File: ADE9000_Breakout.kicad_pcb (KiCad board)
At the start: 2 copper layers, 38.1 x 38 mm, 61 parts, among them J1 SPI JST-SH, J2 Current In, J3 Voltage In, U1 ADE9000, Y1 24.576MHz

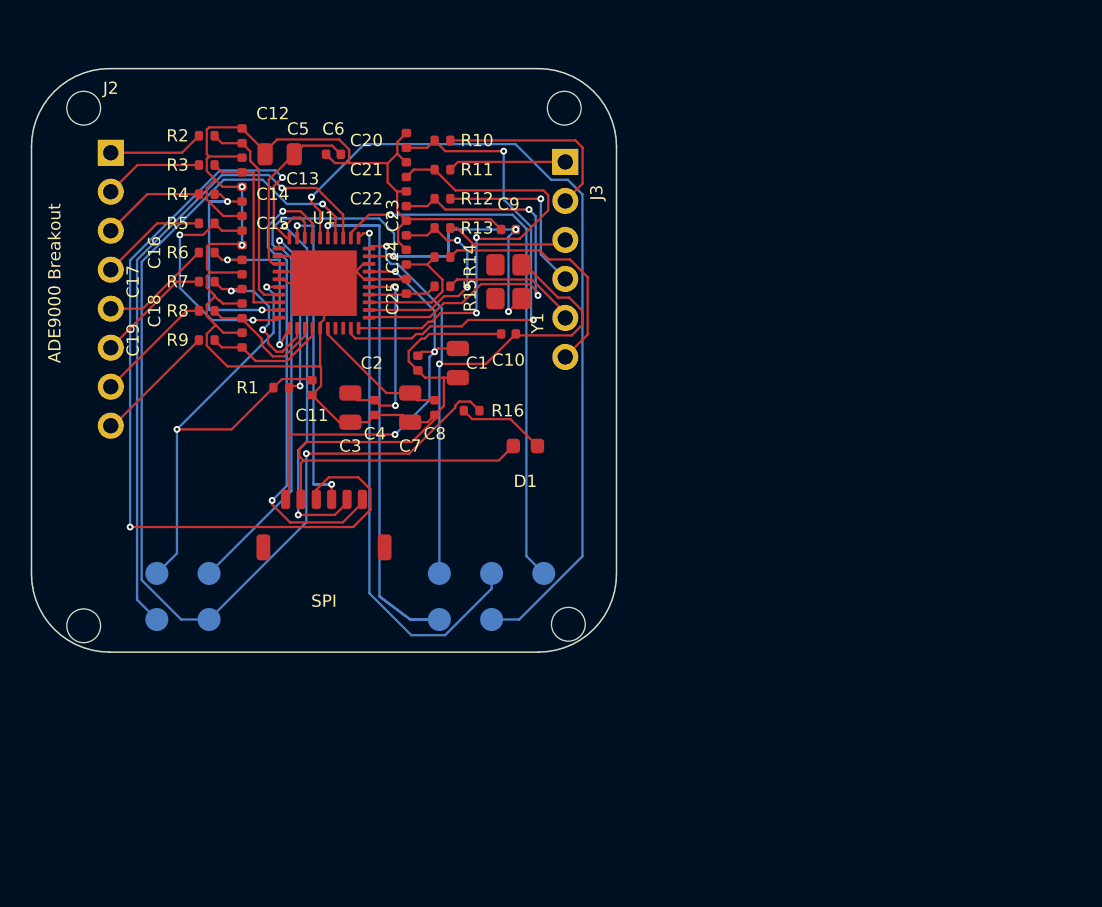
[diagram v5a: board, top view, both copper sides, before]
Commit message: Relayout using connectors for analog inputs
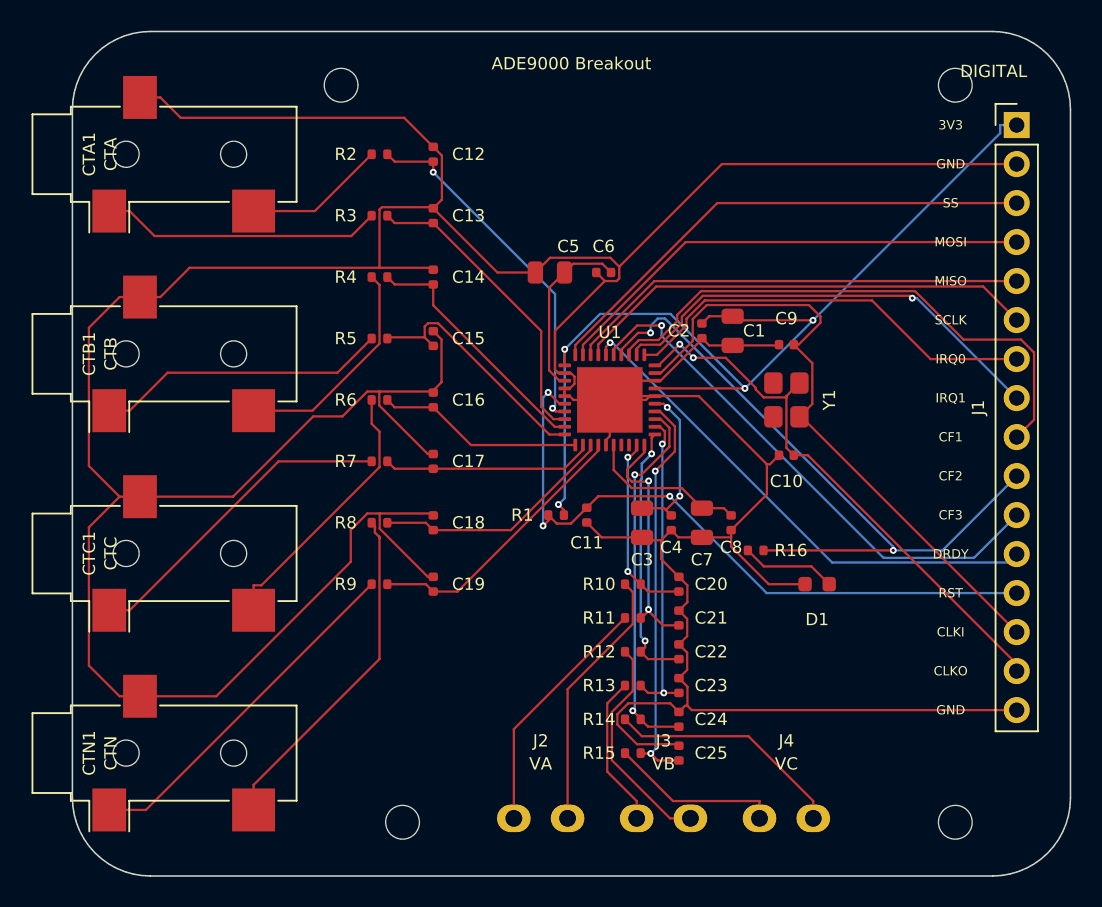
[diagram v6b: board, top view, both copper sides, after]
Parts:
- removed TP10: CF4_DREADY, TestPoint:TestPoint_Pad_D1.5mm
- removed TP11: RESET, TestPoint:TestPoint_Pad_D1.5mm
- removed TP12: CLKIN, TestPoint:TestPoint_Pad_D1.5mm
- removed TP13: CLKOUT, TestPoint:TestPoint_Pad_D1.5mm
- removed TP5: IRQ0, TestPoint:TestPoint_Pad_D1.5mm
- removed TP6: IRQ1, TestPoint:TestPoint_Pad_D1.5mm
- removed TP7: CF1, TestPoint:TestPoint_Pad_D1.5mm
- removed TP8: CF2, TestPoint:TestPoint_Pad_D1.5mm
- removed TP9: CF3_ZX, TestPoint:TestPoint_Pad_D1.5mm
- added CTA1: CT stereo, Jack_3.5mm_CUI_SJ-3523-SMT_Horizontal, F.Cu at (129.5, 88.0)
- added CTB1: CT stereo, Jack_3.5mm_CUI_SJ-3523-SMT_Horizontal, F.Cu at (129.5, 101.0)
- added CTC1: CT stereo, Jack_3.5mm_CUI_SJ-3523-SMT_Horizontal, F.Cu at (129.5, 114.0)
- added CTN1: CT stereo, Jack_3.5mm_CUI_SJ-3523-SMT_Horizontal, F.Cu at (129.5, 127.0)
- added J4: Voltage, TerminalBlock_4Ucon:TerminalBlock_4Ucon_1x02_P3.50mm_Horizontal, F.Cu at (170.0, 131.2)
- J1: value SPI JST-SH -> DIGITAL; footprint JST_SHL_SM06B-SHLS-TF_1x06-1MP_P1.00mm_Horizontal -> PinHeader_1x16_P2.54mm_Vertical
- J2: value Current In -> Voltage; footprint Connector_PinHeader_2.54mm:PinHeader_1x08_P2.54mm_Vertical -> TerminalBlock_4Ucon:TerminalBlock_4Ucon_1x02_P3.50mm_Horizontal
- J3: value Voltage In -> Voltage; footprint Connector_PinHeader_2.54mm:PinHeader_1x06_P2.54mm_Vertical -> TerminalBlock_4Ucon:TerminalBlock_4Ucon_1x02_P3.50mm_Horizontal
- moved J1 52.1 mm to (185.0, 86.1)
- moved J2 51.6 mm to (154.0, 131.2)
- moved J3 43.2 mm to (162.0, 131.2)
- moved C25 35.2 mm to (163.0, 127.0)
- moved C24 34.9 mm to (163.0, 124.8)
- moved C23 34.7 mm to (163.0, 122.6)
- moved C22 34.4 mm to (163.0, 120.4)
- moved C21 34.2 mm to (163.0, 118.2)
- moved C20 33.9 mm to (163.0, 116.0)
- moved R15 32.8 mm to (160.0, 127.0), turned to 0 degrees
- moved R14 32.6 mm to (160.0, 124.8), turned to 0 degrees
- moved R13 32.3 mm to (160.0, 122.6), turned to 0 degrees
- moved R12 32.0 mm to (160.0, 120.4), turned to 0 degrees
- moved R11 31.7 mm to (160.0, 118.2), turned to 0 degrees
- moved R10 31.4 mm to (160.0, 116.0), turned to 0 degrees
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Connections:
- J2 pad 1: IAP_J -> VAP_J
- J2 pad 2: IAN_J -> VAN_J
- J3 pad 1: VAP_J -> VBP_J
- J3 pad 2: VAN_J -> VBN_J
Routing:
- net GND: track 144.9 -> 306.8 mm, vias 2 -> 0
- net CF2: track 69.8 -> 44.1 mm
- net SS: track 56.9 -> 33.2 mm, vias 2 -> 0
- net +3V3: track 42.9 -> 65.4 mm, vias 5 -> 4
- net VCP: track 4.49 -> 26.4 mm, vias 0 -> 2
- net CF4_DREADY: track 54.5 -> 33.5 mm
- net VAN: track 31.5 -> 12.4 mm
- net CLKIN: track 58.9 -> 42.0 mm, vias 3 -> 0
- net INN_J: track 8.05 -> 23.2 mm
- net VCN: track 9.27 -> 24.3 mm, vias 0 -> 2
- net INP_J: track 7.79 -> 22.3 mm
- net VAP: track 29.6 -> 15.6 mm
- net ICN_J: track 7.52 -> 21.1 mm
- net RESET: track 33.0 -> 45.0 mm, vias 2 -> 3
- net IBN_J: track 6.99 -> 19.0 mm
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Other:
- board size 38.1 x 38 mm -> 65 x 55 mm
- board text added: "CF3"
- board text added: "CLKI"
- board text added: "CLKO"
- board text added: "CTA"
- board text added: "CTB"
- board text added: "CTC"
- board text added: "CTN"
- board text added: "DIGITAL"
- board text added: "RST"
- board text added: "VA"
- board text added: "VB"
- board text added: "VC"
- board text removed: "CF3/ZX"
- board text removed: "CLKIN"
- board text removed: "CLKOUT"
- board text removed: "RESET"
- board text removed: "SPI"

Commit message: Rerouted with Groundplanes and new skills
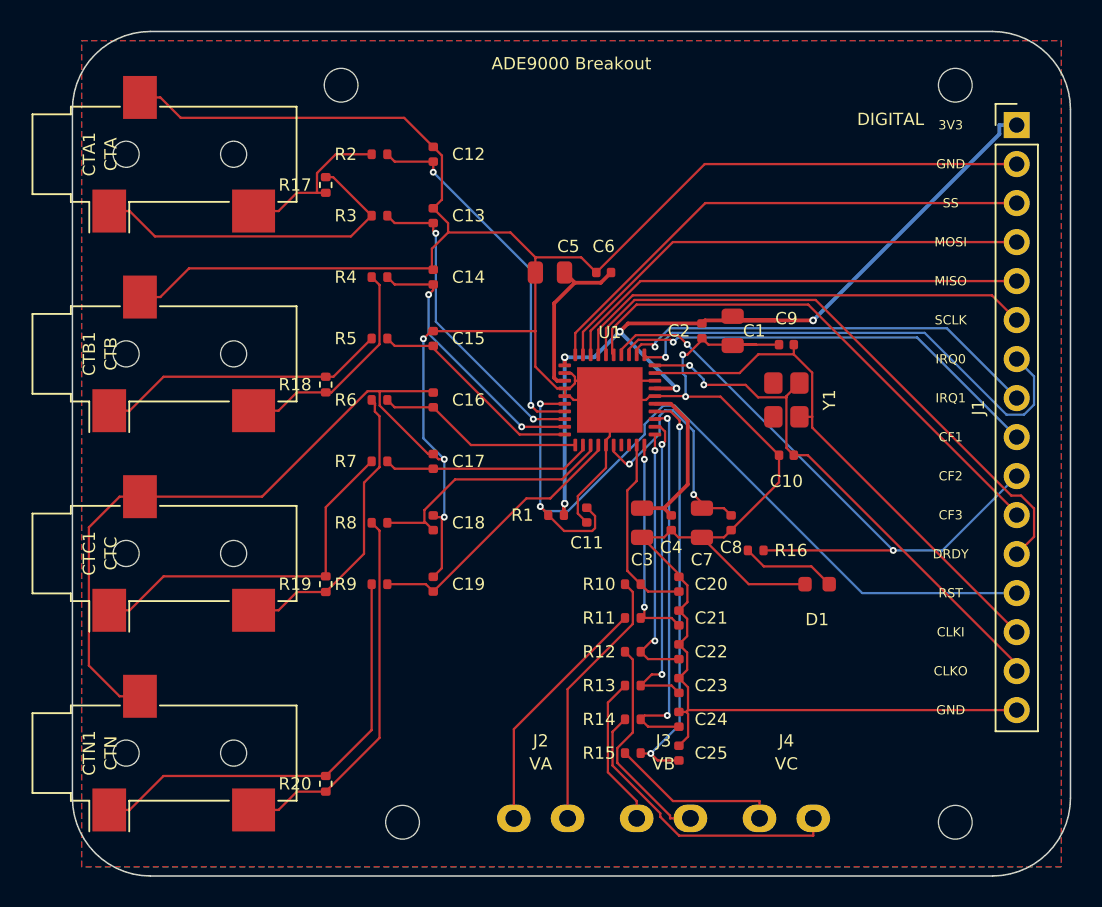
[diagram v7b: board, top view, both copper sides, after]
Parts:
- added R17: 2.4R, R_0402_1005Metric, F.Cu at (140.0, 90.0)
- added R18: 2.4R, R_0402_1005Metric, F.Cu at (140.0, 103.0)
- added R19: 2.4R, R_0402_1005Metric, F.Cu at (140.0, 116.0)
- added R20: 2.4R, R_0402_1005Metric, F.Cu at (140.0, 129.0)
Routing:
- net GND: track 306.8 -> 273.5 mm, vias 0 -> 5
- net +3V3: track 65.4 -> 56.4 mm, vias 4 -> 5
- net RESET: track 45.0 -> 53.6 mm, vias 3 -> 2
- net CF1: track 36.2 -> 28.8 mm, vias 0 -> 1
- net CLKIN: track 42.0 -> 35.1 mm
- net CF4_DREADY: track 33.5 -> 39.4 mm, vias 1 -> 0
- net INN_J: track 23.2 -> 28.7 mm
- net REF: track 10.5 -> 16.0 mm, vias 0 -> 2
- net IRQ0: track 27.5 -> 32.7 mm, vias 0 -> 1
- net IAN_J: track 18.3 -> 22.4 mm
- net VCN_J: track 15.6 -> 19.6 mm
- net ICN_J: track 21.1 -> 23.7 mm
- net INP_J: track 22.3 -> 24.4 mm
- net IBN: track 16.2 -> 14.2 mm
- net ICP_J: track 17.6 -> 19.4 mm
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- added copper zone on B.Cu, net GND
- added copper zone on F.Cu, net GND

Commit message: Added License
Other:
- board text added: "by Tisham Dhar https://whatnick.com v0.1 09/05/2026 TAPR OHL"
- board text removed: "by Tisham Dhar https://whatnick.com v0.1 09/05/2026"
